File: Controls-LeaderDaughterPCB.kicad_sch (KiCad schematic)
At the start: 31 parts, among them U8 LMC555xM

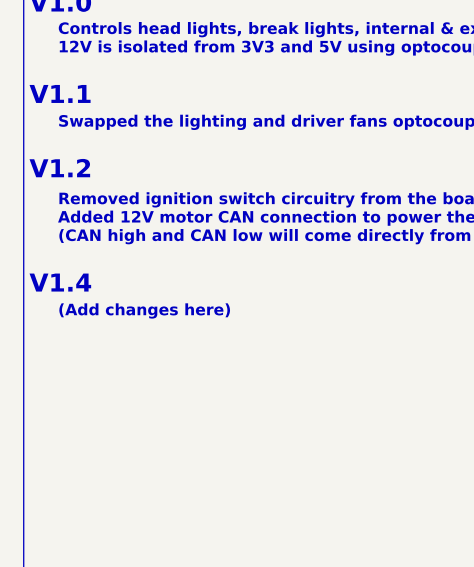
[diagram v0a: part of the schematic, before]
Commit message: Changed optocoupler resistor values, updated Mouser PNs
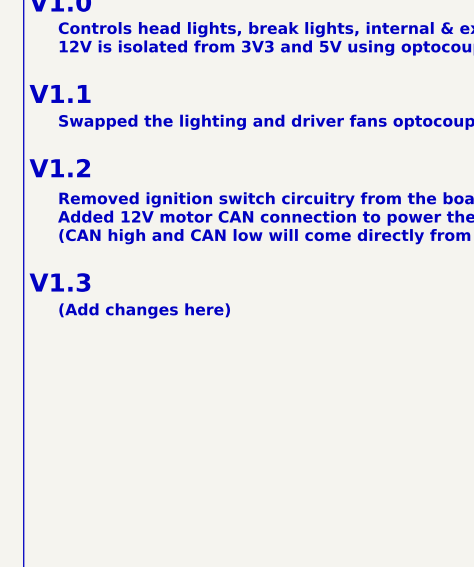
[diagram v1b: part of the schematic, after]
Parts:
- C13: Mauser PN 81-GRM21BR61A476ME5L -> (none); Mouser PN (none) -> 81-GRM21BR61A476ME5L
- C14: Mauser PN 80-C0805C103J5R -> (none); Mouser PN (none) -> 80-C0805C103J5R
- C6: Mauser PN 80-C0805C105K5P -> (none); Mouser PN (none) -> 80-C0805C105K5P
- C6: Mauser PN 80-C0805C104K3R -> (none); Mouser PN (none) -> 80-C0805C104K3R
- D3: Mauser PN 621-BAV16W-F -> (none); Mouser PN (none) -> 621-BAV16W-F
- DISP1: Mauser PN 538-43650-0415 -> (none); Mouser PN (none) -> 538-43650-0415
- HZD_SW1, IG1: Mouser PN (none) -> 538-43650-0215
- R14: Mauser PN 603-RP0805BRD0720KL -> (none); Mouser PN (none) -> 603-RP0805BRD0720KL
- R31: Mauser PN 71-CRCW08051K00FKEAC -> (none); Mouser PN (none) -> 71-CRCW08051K00FKEAC
- SOM1, SOM2: Mauser PN 538-52465-2070 -> (none); Mouser PN (none) -> 538-52465-2070
- Turn_Signal_SW1: Mauser PN 538-43650-0315 -> (none); Mouser PN (none) -> 538-43650-0315
- U8: Mauser PN 595-LMC555IMX/NOPB -> (none); Mouser PN (none) -> 595-LMC555IMX/NOPB
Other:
- note added: "V1.3"
- note removed: "V1.4"
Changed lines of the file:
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@@
     (effects (font (size 2 2) (thickness 0.4) bold) (justify left bottom))
   )
-  (text "V1.4" (at 13.335 163.83 0)
+  (text "V1.3" (at 13.335 163.83 0)
     (effects (font (size 2 2) (thickness 0.4) bold) (justify left bottom))
   )
@@
       (effects (font (size 1.27 1.27)) hide)
     )
+    (property "Mouser PN" "538-43650-0215" (at 176.53 110.49 0)
+      (effects (font (size 1.27 1.27)) hide)
+    )
     (pin "1")
     (pin "2")
@@
       (effects (font (size 1.27 1.27)) hide)
     )
-    (property "Mauser PN" "81-GRM21BR61A476ME5L" (at 147.955 107.95 0)
+    (property "Mouser PN" "81-GRM21BR61A476ME5L" (at 147.955 107.95 0)
       (effects (font (size 1.27 1.27)) hide)
     )
@@
       (effects (font (size 1.27 1.27)) hide)
     )
-    (property "Mauser PN" "80-C0805C105K5P" (at 92.71 107.315 0)
+    (property "Mouser PN" "80-C0805C105K5P" (at 92.71 107.315 0)
       (effects (font (size 1.27 1.27)) hide)
     )
@@
       (effects (font (size 1.27 1.27)) hide)
     )
-    (property "Mauser PN" "621-BAV16W-F" (at 187.96 106.045 0)
+    (property "Mouser PN" "621-BAV16W-F" (at 187.96 106.045 0)
       (effects (font (size 1.27 1.27)) hide)
     )
@@
       (effects (font (size 1.27 1.27)) hide)
     )
-    (property "Mauser PN" "538-43650-0315" (at 175.26 90.805 0)
+    (property "Mouser PN" "538-43650-0315" (at 175.26 90.805 0)
       (effects (font (size 1.27 1.27)) hide)
     )
@@
       (effects (font (size 1.27 1.27)) hide)
     )
+    (property "Mouser PN" "538-43650-0215" (at 254 120.015 0)
+      (effects (font (size 1.27 1.27)) hide)
+    )
     (pin "1")
     (pin "2")
@@
       (effects (font (size 1.27 1.27)) hide)
     )
-    (property "Mauser PN" "603-RP0805BRD0720KL" (at 147.955 100.965 0)
+    (property "Mouser PN" "603-RP0805BRD0720KL" (at 147.955 100.965 0)
       (effects (font (size 1.27 1.27)) hide)
     )
@@
       (effects (font (size 1.27 1.27)) hide)
     )
-    (property "Mauser PN" "80-C0805C104K3R" (at 101.6 107.315 0)
-      (effects (font (size 1.27 1.27)) hide)
-    )
     (property "PN" "C0805C104K3RACTU" (at 101.6 107.315 0)
+      (effects (font (size 1.27 1.27)) hide)
+    )
+    (property "Mouser PN" "80-C0805C104K3R" (at 101.6 107.315 0)
       (effects (font (size 1.27 1.27)) hide)
     )
@@
       (effects (font (size 1.27 1.27)) hide)
     )
-    (property "Mauser PN" "80-C0805C103J5R" (at 106.68 107.315 0)
+    (property "Mouser PN" "80-C0805C103J5R" (at 106.68 107.315 0)
       (effects (font (size 1.27 1.27)) hide)
     )
@@
       (effects (font (size 1.27 1.27)) (justify left top) hide)
     )
-    (property "Mauser PN" "538-52465-2070" (at 156.845 46.355 0)
-      (effects (font (size 1.27 1.27)) hide)
-    )
     (property "PN" "52465-2070" (at 156.845 46.355 0)
+      (effects (font (size 1.27 1.27)) hide)
+    )
+    (property "Mouser PN" "538-52465-2070" (at 156.845 46.355 0)
       (effects (font (size 1.27 1.27)) hide)
     )
@@
       (effects (font (size 1.27 1.27)) hide)
     )
-    (property "Mauser PN" "538-43650-0415" (at 254 86.36 0)
+    (property "Mouser PN" "538-43650-0415" (at 254 86.36 0)
       (effects (font (size 1.27 1.27)) hide)
     )
@@
       (effects (font (size 1.27 1.27)) (justify left top) hide)
     )
-    (property "Mauser PN" "538-52465-2070" (at 243.205 46.355 0)
-      (effects (font (size 1.27 1.27)) hide)
-    )
     (property "PN" "52465-2070" (at 243.205 46.355 0)
+      (effects (font (size 1.27 1.27)) hide)
+    )
+    (property "Mouser PN" "538-52465-2070" (at 243.205 46.355 0)
       (effects (font (size 1.27 1.27)) hide)
     )
@@
       (effects (font (size 1.27 1.27)) hide)
     )
-    (property "Mauser PN" "595-LMC555IMX/NOPB" (at 122.555 98.425 0)
-      (effects (font (size 1.27 1.27)) hide)
-    )
     (property "PN" "LMC555IMX/NOPB" (at 122.555 98.425 0)
+      (effects (font (size 1.27 1.27)) hide)
+    )
+    (property "Mouser PN" "595-LMC555IMX/NOPB" (at 122.555 98.425 0)
       (effects (font (size 1.27 1.27)) hide)
     )
@@
       (effects (font (size 1.27 1.27)) hide)
     )
-    (property "Mauser PN" "621-BAV16W-F" (at 187.96 114.935 0)
+    (property "Mouser PN" "621-BAV16W-F" (at 187.96 114.935 0)
       (effects (font (size 1.27 1.27)) hide)
     )
@@
       (effects (font (size 1.27 1.27)) hide)
     )
-    (property "Mauser PN" "71-CRCW08051K00FKEAC" (at 147.955 95.885 0)
-      (effects (font (size 1.27 1.27)) hide)
-    )
+    (property "Mouser PN" "71-CRCW08051K00FKEAC" (at 147.955 95.885 0)
+      (effects (font (size 1.27 1.27)) hide)
+    )

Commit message: Uploaded image for ReadME
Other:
- sheet Ignition Switch renamed Ignition Signals
- sheet Ignition Signals: file ignition_switch.kicad_sch -> ignition_signals.kicad_sch
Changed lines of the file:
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@@
     (stroke (width 0.1524) (type solid))
     (fill (color 0 0 0 0.0000))
-    (property "Sheetname" "Ignition Switch" (at 19.05 48.8184 0)
+    (property "Sheetname" "Ignition Signals" (at 19.05 48.8184 0)
       (effects (font (size 1.27 1.27)) (justify left bottom))
     )
-    (property "Sheetfile" "ignition_switch.kicad_sch" (at 19.05 55.1946 0)
+    (property "Sheetfile" "ignition_signals.kicad_sch" (at 19.05 55.1946 0)
       (effects (font (size 1.27 1.27)) (justify left top))
     )

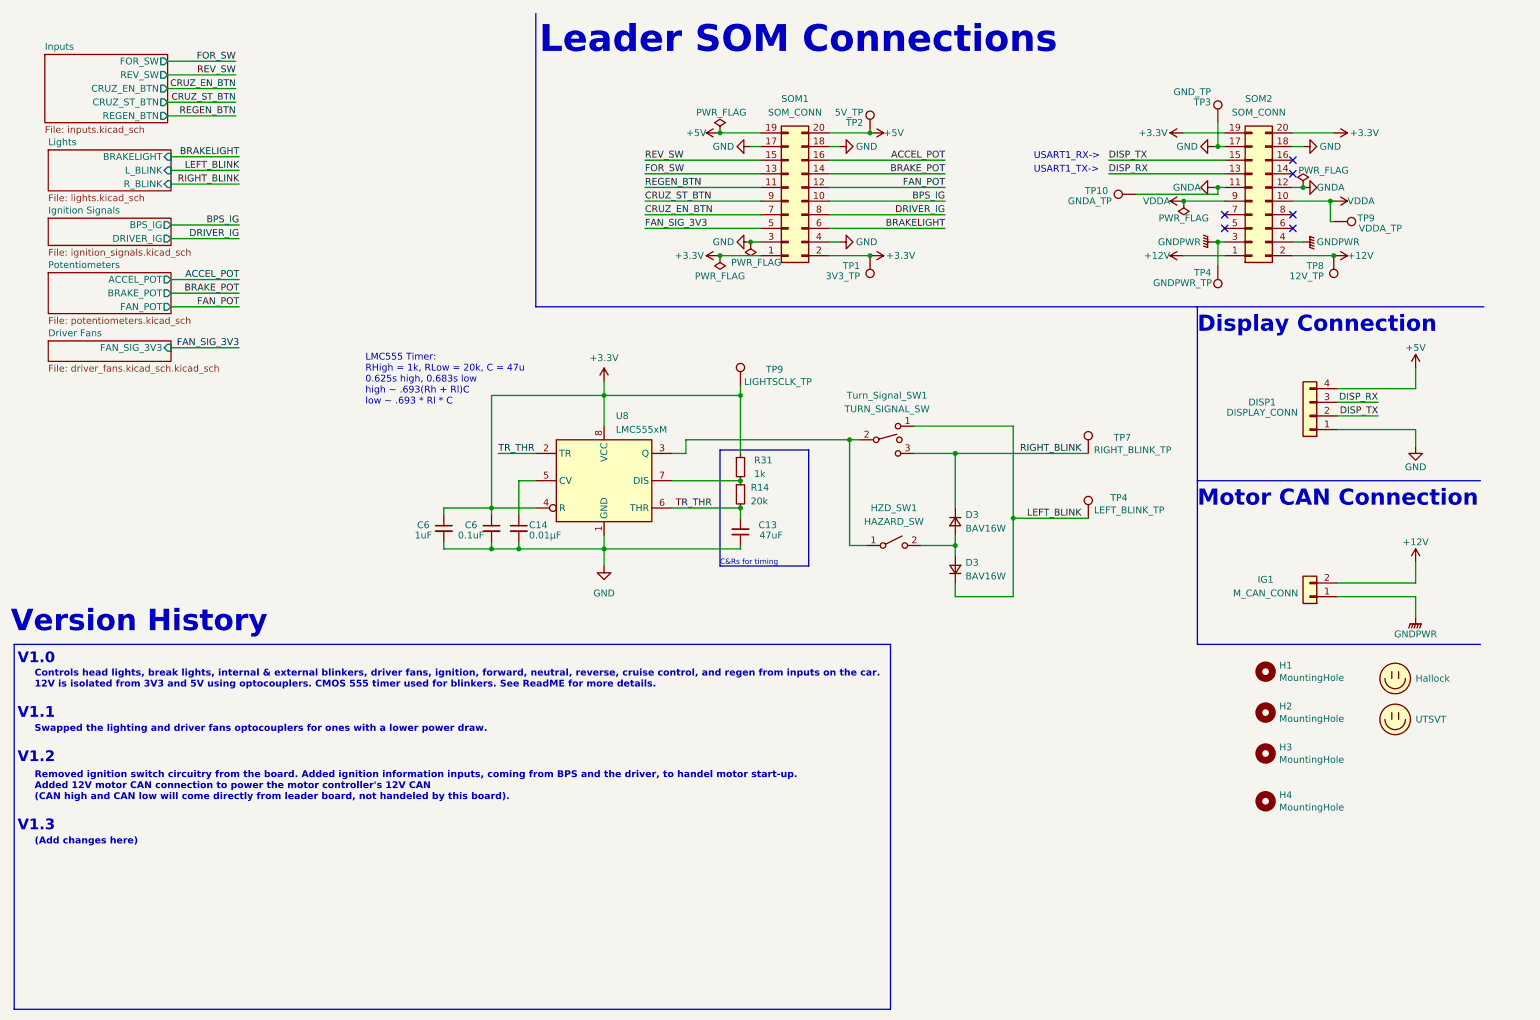
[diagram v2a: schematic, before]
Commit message: Fixed leaderSOM connections, removed optocouplers for lighting and fans, found new MOSFETs
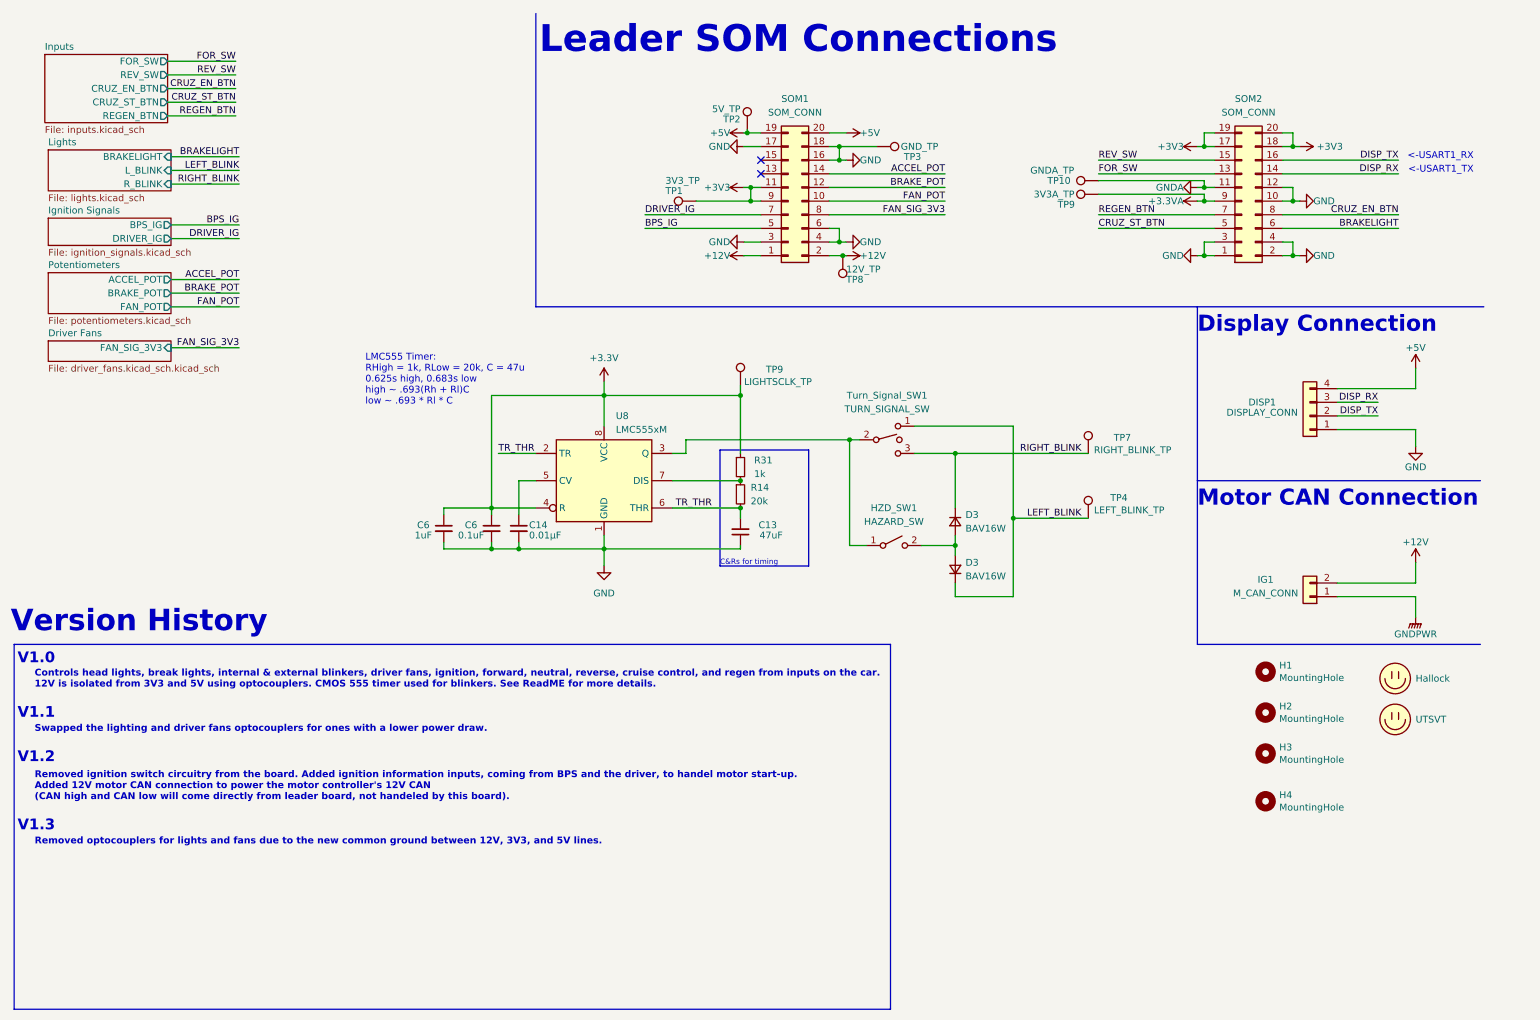
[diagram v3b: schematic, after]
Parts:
- removed TP4: GNDPWR_TP, TestPoint:TestPoint_Pad_1.5x1.5mm, symbol Connector:TestPoint
- TP9: value VDDA_TP -> 3V3A_TP
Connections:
- net +12V: now also SOM1.1 (Pin_1), SOM1.2 (Pin_2); no longer SOM2.1 (Pin_1), SOM2.2 (Pin_2)
- net +3.3V: no longer SOM1.1 (Pin_1), SOM1.2 (Pin_2), SOM2.19 (Pin_19), SOM2.20 (Pin_20), TP1.1
- net ACCEL_POT: now also SOM1.14 (Pin_14); no longer SOM1.16 (Pin_16)
- net BPS_IG: now also SOM1.5 (Pin_5); no longer SOM1.10 (Pin_10)
- net BRAKELIGHT: now also SOM2.6 (Pin_6); no longer SOM1.6 (Pin_6)
- net BRAKE_POT: now also SOM1.12 (Pin_12); no longer SOM1.14 (Pin_14)
- net CRUZ_EN_BTN: now also SOM2.8 (Pin_8); no longer SOM1.7 (Pin_7)
- net CRUZ_ST_BTN: now also SOM2.5 (Pin_5); no longer SOM1.9 (Pin_9)
- net DISP_RX: now also SOM2.14 (Pin_14); no longer SOM2.13 (Pin_13)
- net DISP_TX: now also SOM2.16 (Pin_16); no longer SOM2.15 (Pin_15)
- net DRIVER_IG: now also SOM1.7 (Pin_7); no longer SOM1.8 (Pin_8)
- net FAN_POT: now also SOM1.10 (Pin_10); no longer SOM1.12 (Pin_12)
- net FAN_SIG_3V3: now also SOM1.8 (Pin_8); no longer SOM1.5 (Pin_5)
- net FOR_SW: now also SOM2.13 (Pin_13); no longer SOM1.13 (Pin_13)
- net GND: now also SOM1.16 (Pin_16), SOM1.6 (Pin_6), SOM2.1 (Pin_1), SOM2.10 (Pin_10), SOM2.12 (Pin_12), SOM2.2 (Pin_2), SOM2.3 (Pin_3), SOM2.4 (Pin_4); no longer SOM2.17 (Pin_17), SOM2.18 (Pin_18)
- net GNDA: no longer SOM2.12 (Pin_12)
- net GNDPWR: no longer SOM2.3 (Pin_3), SOM2.4 (Pin_4)
- net REGEN_BTN: now also SOM2.7 (Pin_7); no longer SOM1.11 (Pin_11)
- net REV_SW: now also SOM2.15 (Pin_15); no longer SOM1.15 (Pin_15)
- net VDDA renamed +3.3VA
- net +3.3VA: no longer SOM2.10 (Pin_10)
- new net +3V3: SOM1.11 (Pin_11), SOM1.9 (Pin_9), SOM2.17 (Pin_17), SOM2.18 (Pin_18), SOM2.19 (Pin_19), SOM2.20 (Pin_20), TP1.1
- no-connect marks 6 -> 2
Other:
- note added: "<-USART1_RX"
- note added: "<-USART1_TX"
- note added: "Removed optocouplers for lights and fans due to the new common ground between 12V, 3V3, and 5V lines."
- note removed: "(Add changes here)"
- note removed: "USART1_RX->"
- note removed: "USART1_TX->"
- moved on the sheet: SOM2, TP1, TP10, TP2, TP3, TP8, TP9
